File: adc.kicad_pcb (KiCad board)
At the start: 2 copper layers, 53.8 x 69.1 mm, 86 parts, among them J1 Conn_02x08_Odd_Even, J2 Conn_02x08_Odd_Even, J3 Conn_02x08_Odd_Even, J4 Conn_02x08_Odd_Even, J5 Conn_01x04_Male, J9 Conn_02x08_Odd_Even, U1 ADC128D818, U2 ADC128D818, U3 ADC128D818, U4 ADC128D818, U5 ADC128D818

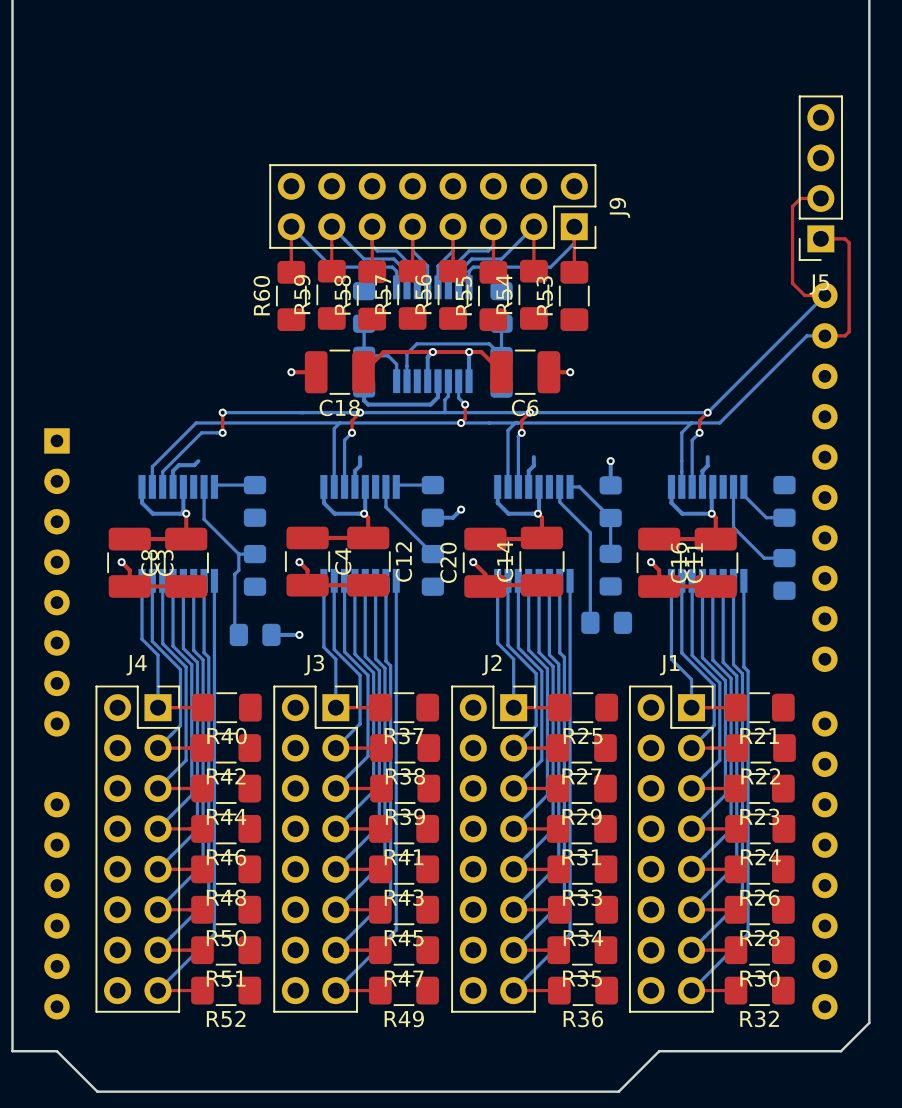
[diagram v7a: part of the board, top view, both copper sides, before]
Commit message: Replaced female 2x8 headers with male. Female makes more sense on the thermistors
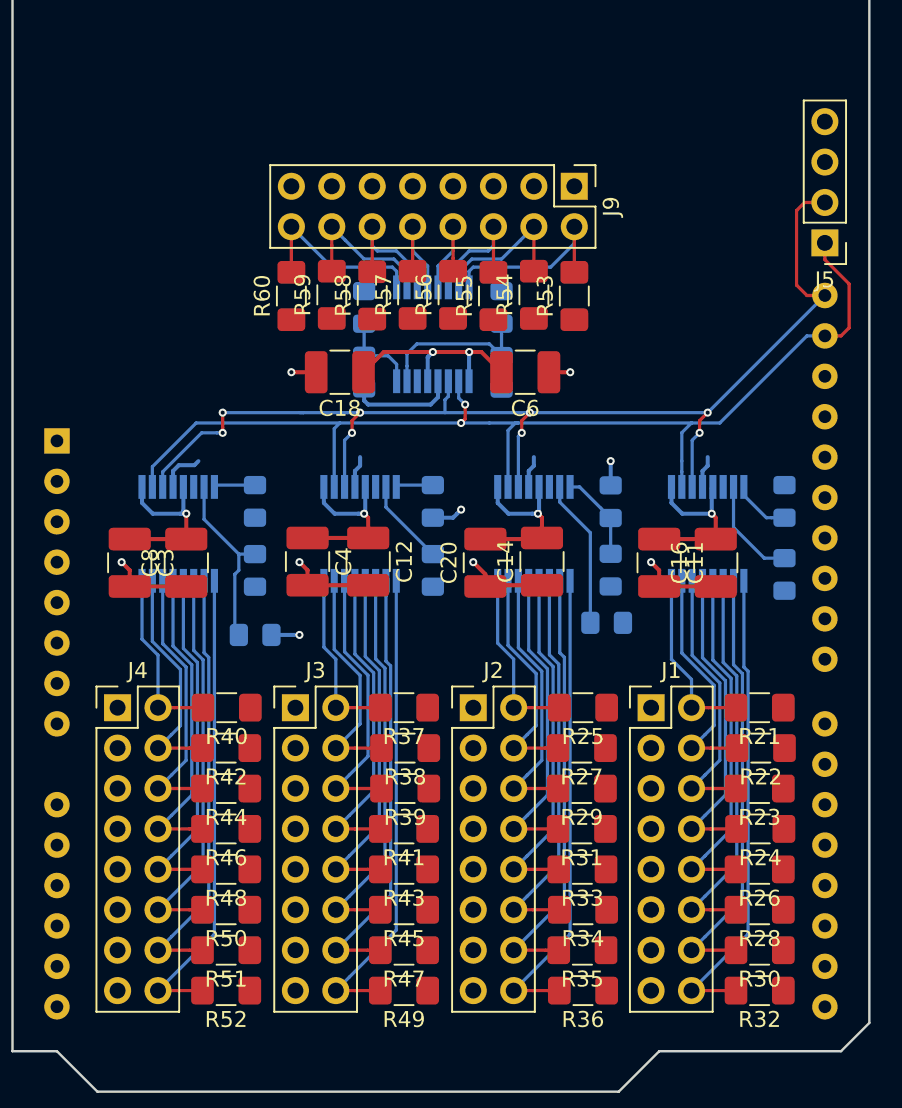
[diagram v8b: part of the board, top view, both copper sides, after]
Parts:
- J1, J2, J3, J4, J9: footprint Connector_PinSocket_2.54mm:PinSocket_2x08_P2.54mm_Vertical -> Connector_PinHeader_2.54mm:PinHeader_2x08_P2.54mm_Vertical
- J5: footprint Connector_PinSocket_2.54mm:PinSocket_1x04_P2.54mm_Vertical -> Connector_PinHeader_2.54mm:PinHeader_1x04_P2.54mm_Vertical
- moved J9 2.54 mm to (247.7, 92.2)
- moved J1 2.54 mm to (252.5, 125.0)
- moved J2 2.54 mm to (241.3, 125.0)
- moved J3 2.54 mm to (230.1, 125.0)
- moved J4 2.54 mm to (218.9, 125.0)
- moved J5 0.36 mm to (263.4, 95.8)
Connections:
- J1 pad 1: Net-(J1-Pad1) -> GND
- J1 pad 10: GND -> Net-(J1-Pad10)
- J1 pad 11: Net-(J1-Pad11) -> GND
- J1 pad 12: GND -> Net-(J1-Pad12)
- J1 pad 13: Net-(J1-Pad13) -> GND
- J1 pad 14: GND -> Net-(J1-Pad14)
- J1 pad 15: Net-(J1-Pad15) -> GND
- J1 pad 16: GND -> Net-(J1-Pad16)
- J1 pad 2: GND -> Net-(J1-Pad2)
- J1 pad 3: Net-(J1-Pad3) -> GND
- J1 pad 4: GND -> Net-(J1-Pad4)
- J1 pad 5: Net-(J1-Pad5) -> GND
- J1 pad 6: GND -> Net-(J1-Pad6)
- J1 pad 7: Net-(J1-Pad7) -> GND
- J1 pad 8: GND -> Net-(J1-Pad8)
- J1 pad 9: Net-(J1-Pad9) -> GND
- J2 pad 1: Net-(J2-Pad1) -> GND
- J2 pad 10: GND -> Net-(J2-Pad10)
- J2 pad 11: Net-(J2-Pad11) -> GND
- J2 pad 12: GND -> Net-(J2-Pad12)
- J2 pad 13: Net-(J2-Pad13) -> GND
- J2 pad 14: GND -> Net-(J2-Pad14)
- J2 pad 15: Net-(J2-Pad15) -> GND
- J2 pad 16: GND -> Net-(J2-Pad16)
- J2 pad 2: GND -> Net-(J2-Pad2)
- J2 pad 3: Net-(J2-Pad3) -> GND
- J2 pad 4: GND -> Net-(J2-Pad4)
- J2 pad 5: Net-(J2-Pad5) -> GND
- J2 pad 6: GND -> Net-(J2-Pad6)
- J2 pad 7: Net-(J2-Pad7) -> GND
- J2 pad 8: GND -> Net-(J2-Pad8)
- J2 pad 9: Net-(J2-Pad9) -> GND
- J3 pad 1: Net-(J3-Pad1) -> GND
- J3 pad 10: GND -> Net-(J3-Pad10)
- J3 pad 11: Net-(J3-Pad11) -> GND
- J3 pad 12: GND -> Net-(J3-Pad12)
- J3 pad 13: Net-(J3-Pad13) -> GND
- J3 pad 14: GND -> Net-(J3-Pad14)
- J3 pad 15: Net-(J3-Pad15) -> GND
- J3 pad 16: GND -> Net-(J3-Pad16)
- J3 pad 2: GND -> Net-(J3-Pad2)
- J3 pad 3: Net-(J3-Pad3) -> GND
- J3 pad 4: GND -> Net-(J3-Pad4)
- J3 pad 5: Net-(J3-Pad5) -> GND
- J3 pad 6: GND -> Net-(J3-Pad6)
- J3 pad 7: Net-(J3-Pad7) -> GND
- J3 pad 8: GND -> Net-(J3-Pad8)
- J3 pad 9: Net-(J3-Pad9) -> GND
- J4 pad 1: Net-(J4-Pad1) -> GND
- J4 pad 10: GND -> Net-(J4-Pad10)
- J4 pad 11: Net-(J4-Pad11) -> GND
- J4 pad 12: GND -> Net-(J4-Pad12)
- J4 pad 13: Net-(J4-Pad13) -> GND
- J4 pad 14: GND -> Net-(J4-Pad14)
- J4 pad 15: Net-(J4-Pad15) -> GND
- J4 pad 16: GND -> Net-(J4-Pad16)
- J4 pad 2: GND -> Net-(J4-Pad2)
- J4 pad 3: Net-(J4-Pad3) -> GND
- J4 pad 4: GND -> Net-(J4-Pad4)
- J4 pad 5: Net-(J4-Pad5) -> GND
- J4 pad 6: GND -> Net-(J4-Pad6)
- J4 pad 7: Net-(J4-Pad7) -> GND
- J4 pad 8: GND -> Net-(J4-Pad8)
- J4 pad 9: Net-(J4-Pad9) -> GND
- J9 pad 1: Net-(J9-Pad1) -> GND
- J9 pad 10: GND -> Net-(J9-Pad10)
- J9 pad 11: Net-(J9-Pad11) -> GND
- J9 pad 12: GND -> Net-(J9-Pad12)
- J9 pad 13: Net-(J9-Pad13) -> GND
- J9 pad 14: GND -> Net-(J9-Pad14)
- J9 pad 15: Net-(J9-Pad15) -> GND
- J9 pad 16: GND -> Net-(J9-Pad16)
- J9 pad 2: GND -> Net-(J9-Pad2)
- J9 pad 3: Net-(J9-Pad3) -> GND
- J9 pad 4: GND -> Net-(J9-Pad4)
- J9 pad 5: Net-(J9-Pad5) -> GND
- J9 pad 6: GND -> Net-(J9-Pad6)
- J9 pad 7: Net-(J9-Pad7) -> GND
- J9 pad 8: GND -> Net-(J9-Pad8)
- J9 pad 9: Net-(J9-Pad9) -> GND
- R21 pad 2: Net-(J1-Pad1) -> Net-(J1-Pad2)
- R22 pad 2: Net-(J1-Pad3) -> Net-(J1-Pad4)
- R23 pad 2: Net-(J1-Pad5) -> Net-(J1-Pad6)
- R24 pad 2: Net-(J1-Pad7) -> Net-(J1-Pad8)
- R25 pad 2: Net-(J2-Pad1) -> Net-(J2-Pad2)
- R26 pad 2: Net-(J1-Pad9) -> Net-(J1-Pad10)
- R27 pad 2: Net-(J2-Pad3) -> Net-(J2-Pad4)
- R28 pad 2: Net-(J1-Pad11) -> Net-(J1-Pad12)
- R29 pad 2: Net-(J2-Pad5) -> Net-(J2-Pad6)
- R30 pad 2: Net-(J1-Pad13) -> Net-(J1-Pad14)
- R31 pad 2: Net-(J2-Pad7) -> Net-(J2-Pad8)
- R32 pad 2: Net-(J1-Pad15) -> Net-(J1-Pad16)
- R33 pad 2: Net-(J2-Pad9) -> Net-(J2-Pad10)
- R34 pad 2: Net-(J2-Pad11) -> Net-(J2-Pad12)
- R35 pad 2: Net-(J2-Pad13) -> Net-(J2-Pad14)
- R36 pad 2: Net-(J2-Pad15) -> Net-(J2-Pad16)
- R37 pad 2: Net-(J3-Pad1) -> Net-(J3-Pad2)
- R38 pad 2: Net-(J3-Pad3) -> Net-(J3-Pad4)
- R39 pad 2: Net-(J3-Pad5) -> Net-(J3-Pad6)
- R40 pad 2: Net-(J4-Pad1) -> Net-(J4-Pad2)
- R41 pad 2: Net-(J3-Pad7) -> Net-(J3-Pad8)
- R42 pad 2: Net-(J4-Pad3) -> Net-(J4-Pad4)
- R43 pad 2: Net-(J3-Pad9) -> Net-(J3-Pad10)
- R44 pad 2: Net-(J4-Pad5) -> Net-(J4-Pad6)
- R45 pad 2: Net-(J3-Pad11) -> Net-(J3-Pad12)
- R46 pad 2: Net-(J4-Pad7) -> Net-(J4-Pad8)
- R47 pad 2: Net-(J3-Pad13) -> Net-(J3-Pad14)
- R48 pad 2: Net-(J4-Pad9) -> Net-(J4-Pad10)
- R49 pad 2: Net-(J3-Pad15) -> Net-(J3-Pad16)
- R50 pad 2: Net-(J4-Pad11) -> Net-(J4-Pad12)
- R51 pad 2: Net-(J4-Pad13) -> Net-(J4-Pad14)
- R52 pad 2: Net-(J4-Pad15) -> Net-(J4-Pad16)
- R53 pad 2: Net-(J9-Pad1) -> Net-(J9-Pad2)
- R54 pad 2: Net-(J9-Pad3) -> Net-(J9-Pad4)
- R55 pad 2: Net-(J9-Pad5) -> Net-(J9-Pad6)
- R56 pad 2: Net-(J9-Pad7) -> Net-(J9-Pad8)
- R57 pad 2: Net-(J9-Pad9) -> Net-(J9-Pad10)
- R58 pad 2: Net-(J9-Pad11) -> Net-(J9-Pad12)
- R59 pad 2: Net-(J9-Pad13) -> Net-(J9-Pad14)
- R60 pad 2: Net-(J9-Pad15) -> Net-(J9-Pad16)
- U1 pad 10: Net-(J1-Pad13) -> Net-(J1-Pad14)
- U1 pad 11: Net-(J1-Pad11) -> Net-(J1-Pad12)
- U1 pad 12: Net-(J1-Pad9) -> Net-(J1-Pad10)
- U1 pad 13: Net-(J1-Pad7) -> Net-(J1-Pad8)
- U1 pad 14: Net-(J1-Pad5) -> Net-(J1-Pad6)
- U1 pad 15: Net-(J1-Pad3) -> Net-(J1-Pad4)
- U1 pad 16: Net-(J1-Pad1) -> Net-(J1-Pad2)
- U1 pad 9: Net-(J1-Pad15) -> Net-(J1-Pad16)
- U2 pad 10: Net-(J2-Pad13) -> Net-(J2-Pad14)
- U2 pad 11: Net-(J2-Pad11) -> Net-(J2-Pad12)
- U2 pad 12: Net-(J2-Pad9) -> Net-(J2-Pad10)
- U2 pad 13: Net-(J2-Pad7) -> Net-(J2-Pad8)
- U2 pad 14: Net-(J2-Pad5) -> Net-(J2-Pad6)
- U2 pad 15: Net-(J2-Pad3) -> Net-(J2-Pad4)
- U2 pad 16: Net-(J2-Pad1) -> Net-(J2-Pad2)
- U2 pad 9: Net-(J2-Pad15) -> Net-(J2-Pad16)
- U3 pad 10: Net-(J3-Pad13) -> Net-(J3-Pad14)
- U3 pad 11: Net-(J3-Pad11) -> Net-(J3-Pad12)
- U3 pad 12: Net-(J3-Pad9) -> Net-(J3-Pad10)
- U3 pad 13: Net-(J3-Pad7) -> Net-(J3-Pad8)
- U3 pad 14: Net-(J3-Pad5) -> Net-(J3-Pad6)
- U3 pad 15: Net-(J3-Pad3) -> Net-(J3-Pad4)
- U3 pad 16: Net-(J3-Pad1) -> Net-(J3-Pad2)
- U3 pad 9: Net-(J3-Pad15) -> Net-(J3-Pad16)
- U4 pad 10: Net-(J4-Pad13) -> Net-(J4-Pad14)
- U4 pad 11: Net-(J4-Pad11) -> Net-(J4-Pad12)
- U4 pad 12: Net-(J4-Pad9) -> Net-(J4-Pad10)
- U4 pad 13: Net-(J4-Pad7) -> Net-(J4-Pad8)
- U4 pad 14: Net-(J4-Pad5) -> Net-(J4-Pad6)
- U4 pad 15: Net-(J4-Pad3) -> Net-(J4-Pad4)
- U4 pad 16: Net-(J4-Pad1) -> Net-(J4-Pad2)
- U4 pad 9: Net-(J4-Pad15) -> Net-(J4-Pad16)
- U5 pad 10: Net-(J9-Pad13) -> Net-(J9-Pad14)
- U5 pad 11: Net-(J9-Pad11) -> Net-(J9-Pad12)
- U5 pad 12: Net-(J9-Pad9) -> Net-(J9-Pad10)
- U5 pad 13: Net-(J9-Pad7) -> Net-(J9-Pad8)
- U5 pad 14: Net-(J9-Pad5) -> Net-(J9-Pad6)
- U5 pad 15: Net-(J9-Pad3) -> Net-(J9-Pad4)
- U5 pad 16: Net-(J9-Pad1) -> Net-(J9-Pad2)
- U5 pad 9: Net-(J9-Pad15) -> Net-(J9-Pad16)
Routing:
- net Net-(J1-Pad16): track 0.00 -> 30.1 mm
- net Net-(J1-Pad15): track 30.1 -> 0.00 mm
- net Net-(J3-Pad16): track 0.00 -> 30.1 mm
- net Net-(J3-Pad15): track 30.1 -> 0.00 mm
- net Net-(J2-Pad16): track 0.00 -> 30.1 mm
- net Net-(J2-Pad15): track 30.1 -> 0.00 mm
- net Net-(J4-Pad16): track 0.00 -> 30.0 mm
- net Net-(J4-Pad15): track 30.0 -> 0.00 mm
- net Net-(J1-Pad14): track 0.00 -> 27.6 mm
- net Net-(J1-Pad13): track 27.6 -> 0.00 mm
- net Net-(J3-Pad14): track 0.00 -> 27.6 mm
- net Net-(J3-Pad13): track 27.6 -> 0.00 mm
- net Net-(J2-Pad14): track 0.00 -> 27.5 mm
- net Net-(J2-Pad13): track 27.5 -> 0.00 mm
- net Net-(J4-Pad14): track 0.00 -> 27.4 mm
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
